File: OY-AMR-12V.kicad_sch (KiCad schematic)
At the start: 26 parts

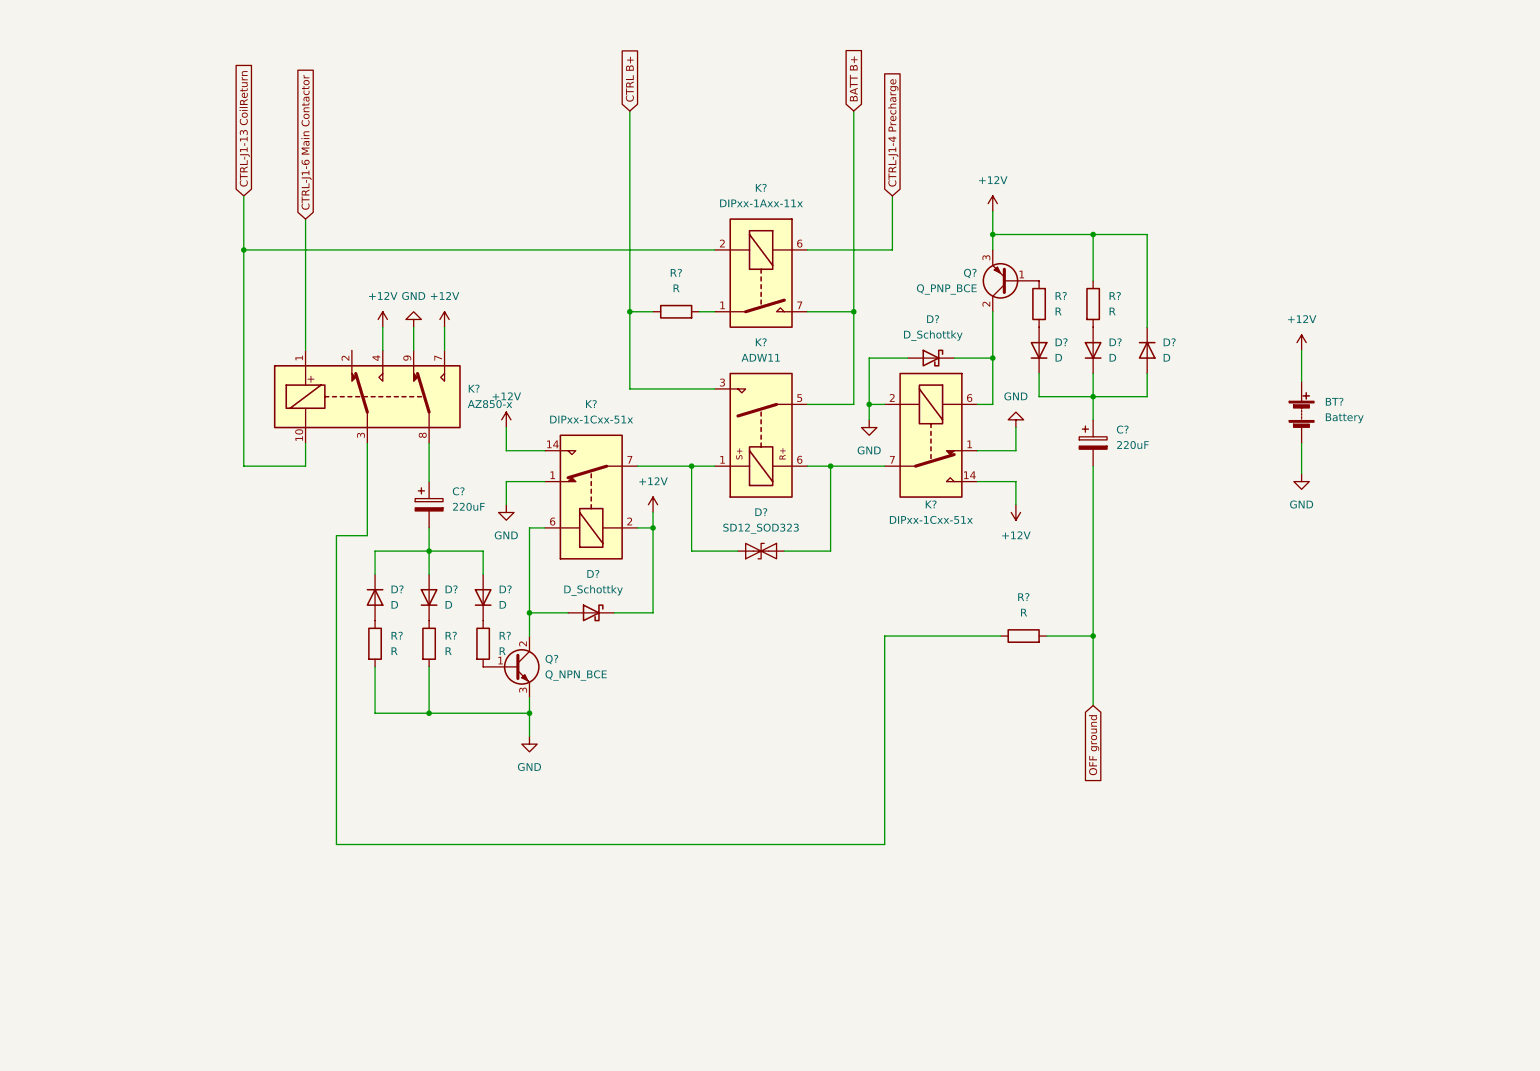
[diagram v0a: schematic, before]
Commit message: Change to relay logic
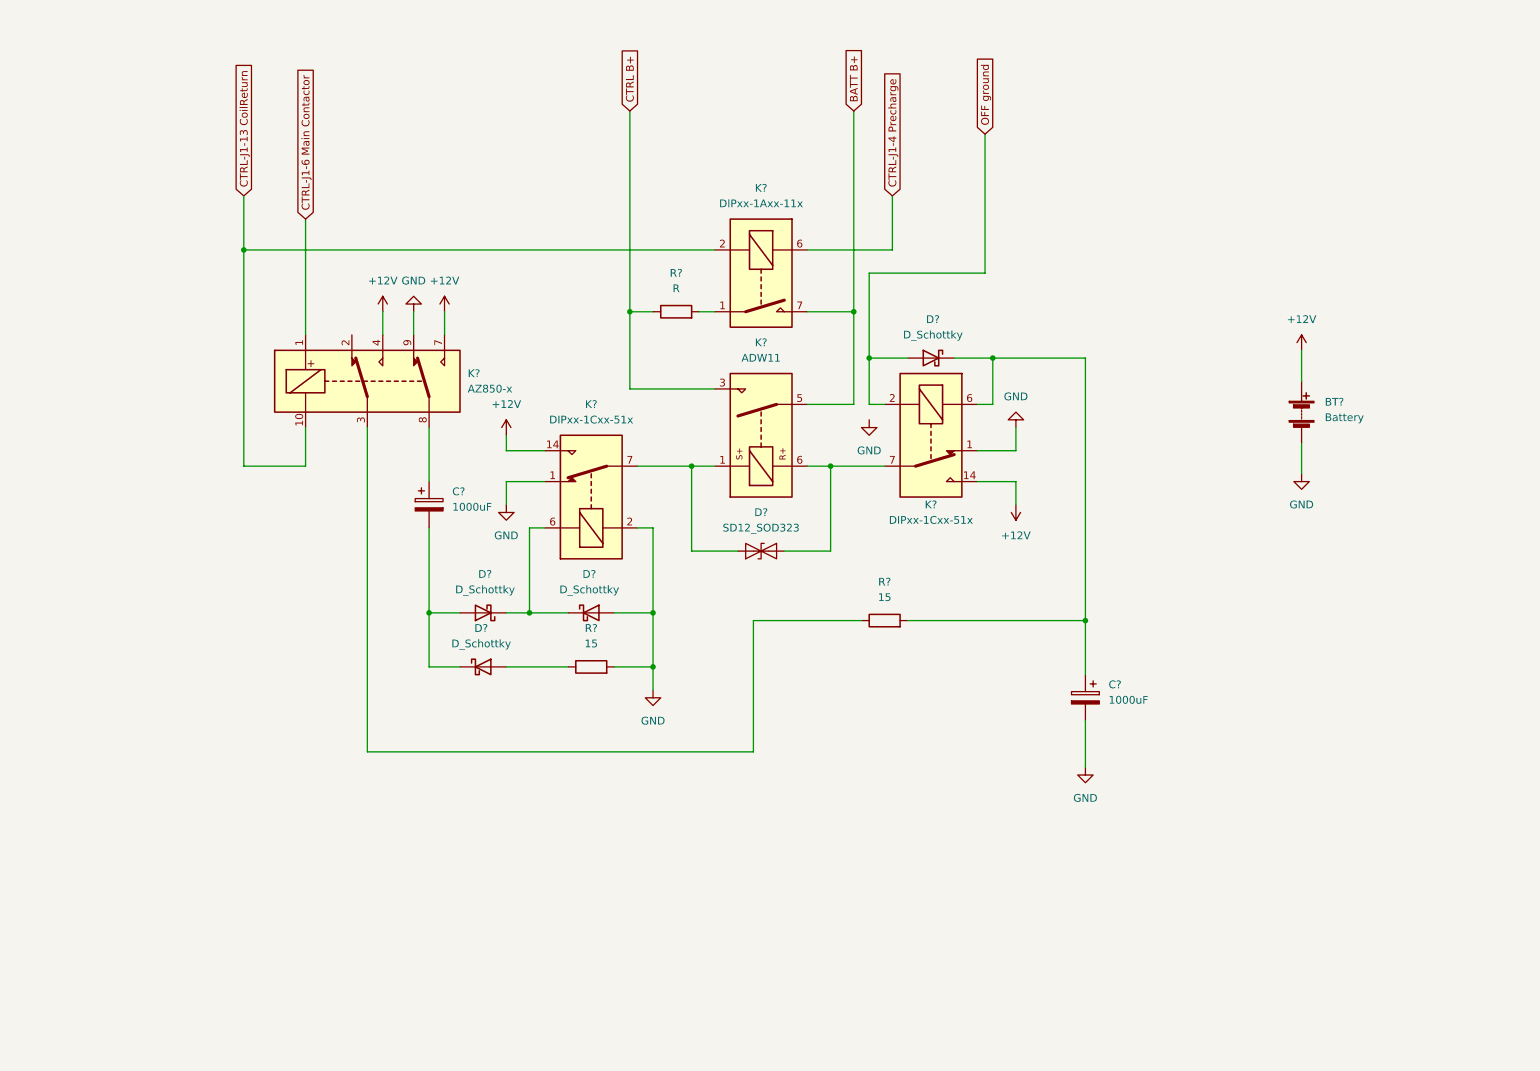
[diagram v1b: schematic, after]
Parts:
- removed D? (x6): D, symbol Device:D
- removed Q?: Q_PNP_BCE, symbol Device:Q_PNP_BCE
- removed Q?: Q_NPN_BCE, symbol Device:Q_NPN_BCE
- removed R? (x5): R, symbol Device:R
- added D? (x2): D_Schottky, symbol Device:D_Schottky
- added R?: 15, symbol Device:R
- C? (x2): value 220uF -> 1000uF
- R?: value R -> 15
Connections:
- net +12V: no longer D?.1 (K), K?.2
- net GND: now also C?.2, D?.2 (A), K?.2, R?.2; no longer D?.2 (A), K?.2
- net OFF ground: now also D?.2 (A), K?.2; no longer C?.2, R?.2
- net at K?.6: now also D?.1 (K), D?.1 (K); no longer D?.2 (A)
- net at C?.2: now also D?.1 (K), D?.2 (A)
- net at C?.1: now also D?.1 (K), K?.6, R?.2
- new net: D?.2 (A), R?.1
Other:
- moved on the sheet: C?, K?, R?

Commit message: Relay-only version in progress
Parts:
- removed K?: ADW11, Relay_THT:Relay_1P1T_NO_10x24x18.8mm_Panasonic_ADW11xxxxW_THT, symbol Relay:ADW11
- removed K?: DIPxx-1Axx-11x, Relay_THT:Relay_StandexMeder_DIP_LowProfile, symbol Relay:DIPxx-1Axx-11x
- removed R?: R, symbol Device:R
- added J? (x2): Main contactor drive, symbol Connector:Conn_01x02_Female
- added J?: 12V battery, symbol Connector:Conn_01x02_Female
- added K?: G8PM-K1A71R, symbol Miscellaneous:G8PM-K1A71R
- added SW?: Keylock switch, symbol Miscellaneous:H200AA2F205NQ
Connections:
- net +12V: now also J?.1 (Pin_1)
- net GND: now also J?.2 (Pin_2)
- net at D?.1 (A1), K?.7, K?.8: now also J?.1 (Pin_1)
- net at D?.2 (A2), K?.7, K?.8: now also J?.2 (Pin_2)
- net CTRL-J1-13 CoilReturn: no longer names the net of K?.10
- net CTRL-J1-13 CoilReturn: now also J?.1 (Pin_1)
- net CTRL-J1-6 Main Contactor: no longer names the net of K?.1
- net CTRL-J1-6 Main Contactor: now also J?.2 (Pin_2)
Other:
- moved on the sheet: BT?, C?, D?, K?, R?

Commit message: Trying out bistable config options
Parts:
- removed BT?: Battery, symbol Device:Battery
- removed SW?: Keylock switch, symbol Miscellaneous:H200AA2F205NQ
- added C? (x2): 6.8mF, symbol Device:C_Polarized_Small
- added D? (x7): SB130-T, symbol Device:D_Schottky_Small
- added F?: Fuse, symbol Device:Fuse
- added R? (x2): 10, symbol Device:R_Small
- added SW?: Keyswitch, symbol Miscellaneous:H200AA2F205NQ
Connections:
- net +12V: now also K?.1, K?.2, F?.2
- net GND: now also C?.2, C?.2, SW?.2 (2a), SW?.4 (4a)
- net at K?.3: now also D?.2 (A)
- net at K?.4: now also K?.5
- net at K?.6: now also D?.2 (A)
- net at K?.7: now also D?.1 (K), D?.1 (K), D?.1 (K), D?.2 (A)
- new net: C?.1, D?.2 (A), R?.1
- new net: D?.1 (K), R?.2
- new net: C?.1, D?.1 (K), R?.1
- new net: D?.2 (A), R?.2
- new net +12P: F?.1, SW?.7 (3b)
- new net GND_OFF: D?.1 (K), D?.1 (K)
- new net KS_AUX+: D?.2 (A), SW?.6 (2b)
- new net KS_OFF-: SW?.1 (1a)
- new net KS_ON+: D?.2 (A), SW?.8 (4b)
- new net KS_ON-: SW?.3 (3a)
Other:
- moved on the sheet: K?

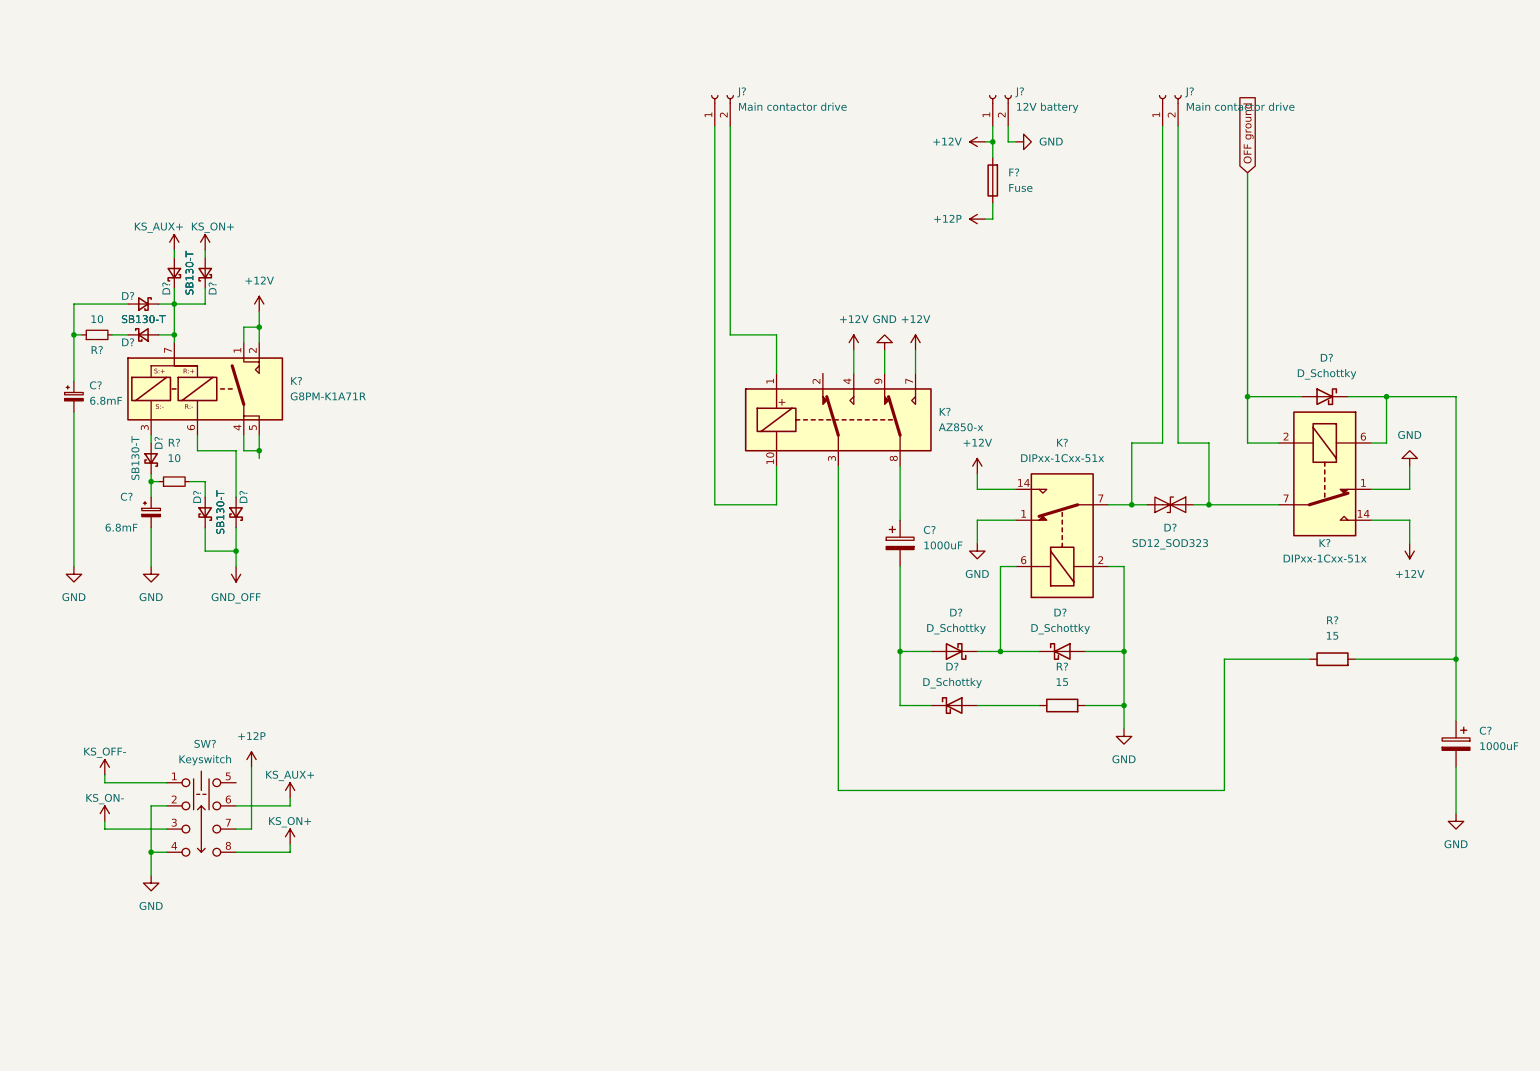
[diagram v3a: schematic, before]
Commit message: Re-implement with single-coil latching relays
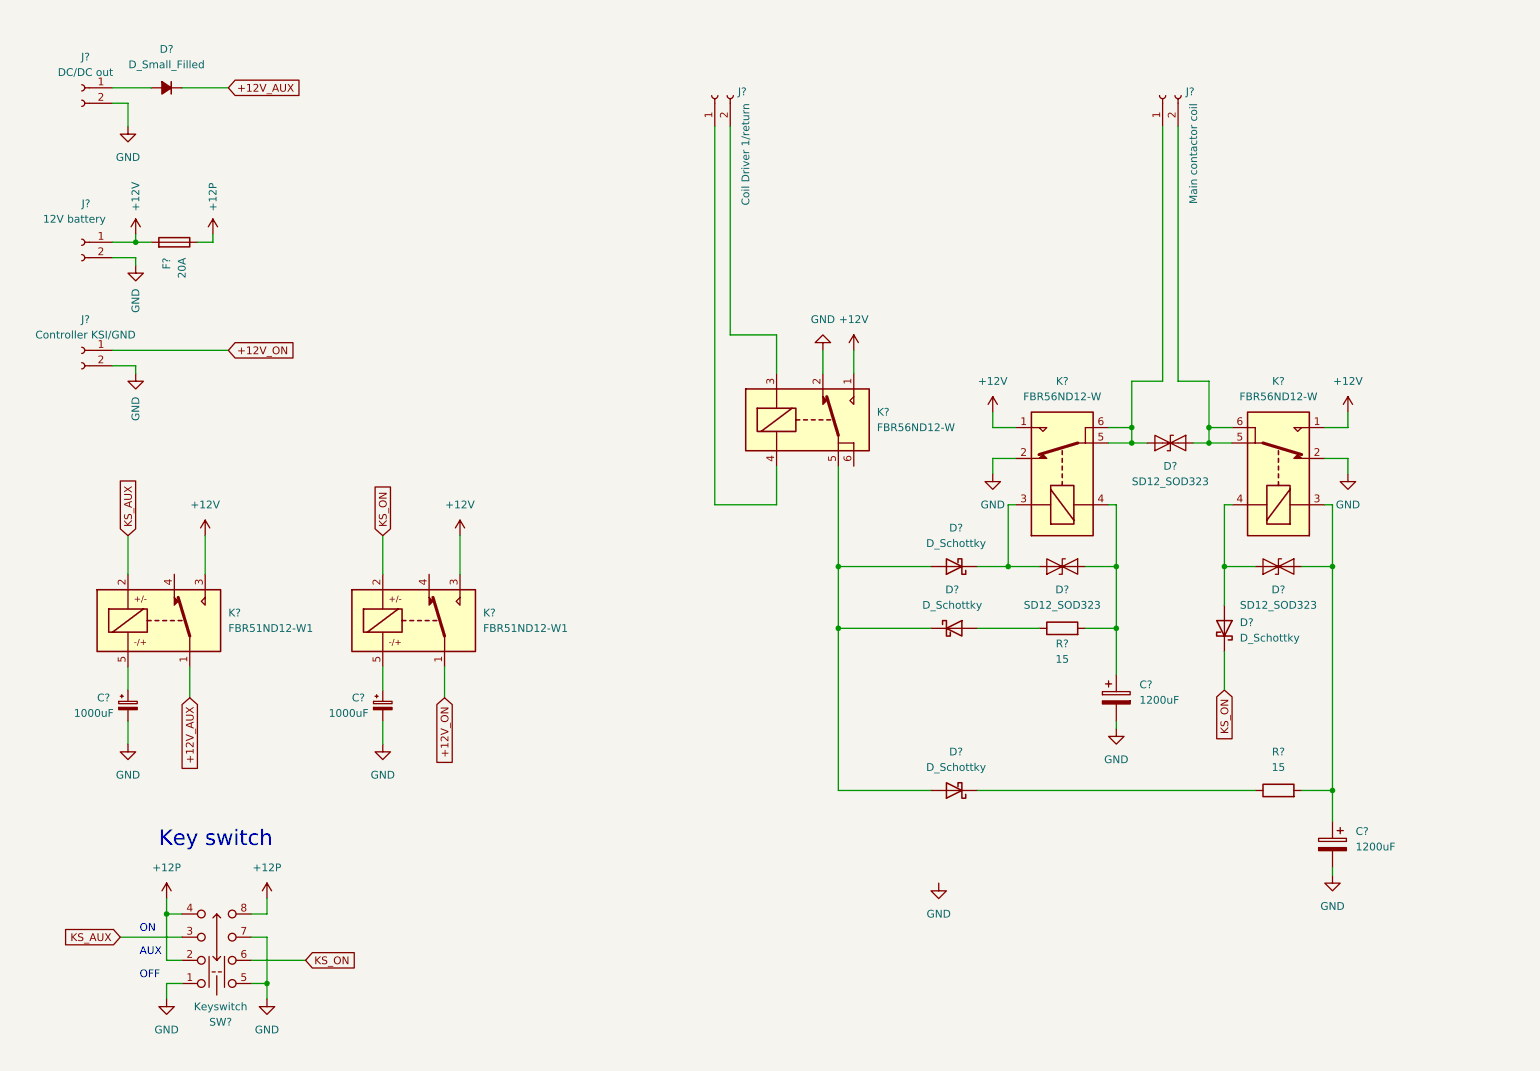
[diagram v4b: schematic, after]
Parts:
- removed C? (x2): 6.8mF, symbol Device:C_Polarized_Small
- removed D? (x7): SB130-T, symbol Device:D_Schottky_Small
- removed D?: D_Schottky, symbol Device:D_Schottky
- removed K?: G8PM-K1A71R, symbol Miscellaneous:G8PM-K1A71R
- removed K? (x2): DIPxx-1Cxx-51x, Relay_THT:Relay_StandexMeder_DIP_LowProfile, symbol Relay:DIPxx-1Cxx-51x
- removed K?: AZ850-x, Relay_THT:Relay_DPDT_FRT5, symbol Relay:AZ850-x
- removed R? (x2): 10, symbol Device:R_Small
- added C? (x2): 1000uF, symbol Device:C_Polarized_Small
- added D?: D_Schottky, symbol Device:D_Schottky
- added D? (x2): SD12_SOD323, Diode_SMD:D_SOD-323, symbol Diode:SD12_SOD323
- added D?: D_Small_Filled, symbol Device:D_Small_Filled
- added J?: Controller KSI/GND, symbol Connector:Conn_01x02_Female
- added J?: DC/DC out, symbol Connector:Conn_01x02_Female
- added K? (x3): FBR56ND12-W, Relay_THT:Relay_SPDT_Omron_G6E, symbol Miscellaneous:FBR56ND12-W
- added K? (x2): FBR51ND12-W1, Relay_THT:Relay_SPDT_Omron_G6E, symbol Miscellaneous:FBR51ND12-W1
- C? (x2): value 1000uF -> 1200uF
- F?: value Fuse -> 20A
- J?: value Main contactor drive -> Coil Driver 1/return
- J?: value Main contactor drive -> Main contactor coil
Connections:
- net KS_OFF- is gone; now on net GND: SW?.1 (1a)
- net KS_ON+ is gone; now on net +12P: SW?.8 (4b)
- net +12P: now also SW?.2 (2a), SW?.4 (4a); no longer SW?.7 (3b)
- net +12V: now also K?.1, K?.1, K?.1, K?.3, K?.3
- net GND: now also C?.2, SW?.5 (1b), SW?.7 (3b), C?.2, C?.2, J?.2 (Pin_2), J?.2 (Pin_2), K?.2, K?.2, K?.2; no longer R?.2, SW?.2 (2a), SW?.4 (4a)
- net at J?.1 (Pin_1): now also K?.4
- net at J?.2 (Pin_2): now also K?.3
- net at D?.1 (K): now also D?.1 (A1), K?.3
- net at D?.1 (A1), J?.1 (Pin_1): now also K?.5, K?.6
- net at C?.1, R?.2: now also D?.2 (A2), K?.3; no longer D?.1 (K)
- net at D?.2 (A2), J?.2 (Pin_2): now also K?.5, K?.6
- net at C?.1: now also R?.2, D?.2 (A2), K?.4
- net at D?.1 (K), D?.2 (A): now also D?.2 (A), K?.5; no longer C?.2
- net at R?.1: now also D?.1 (K)
- net KS_AUX+ renamed KS_ON
- net KS_ON: now also D?.1 (K), K?.2
- net KS_ON- renamed KS_AUX
- net KS_AUX: now also K?.2
- net OFF ground: no longer names the net of D?.2 (A)
- net OFF ground: now also D?.1 (A1), K?.4
- new net: C?.1, K?.5 (x2)
- new net: D?.2 (A), J?.1 (Pin_1)
- new net +12V_AUX: D?.1 (K), K?.1
- new net +12V_ON: J?.1 (Pin_1), K?.1
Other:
- note added: "AUX"
- note added: "Key switch"
- note added: "OFF"
- note added: "ON"
- moved on the sheet: C?, D?, F?, J?, R?, SW?
